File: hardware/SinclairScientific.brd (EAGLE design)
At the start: 47 x 108 mm, 93 parts, among them J1 JSTPH, J3 USB-MICRO, U2 SPX3819-3.3, U3 MCP73831T-2ACI/OT, U4 ATSAMD21G18, U5 W25Q128JVSO, X2 32.768

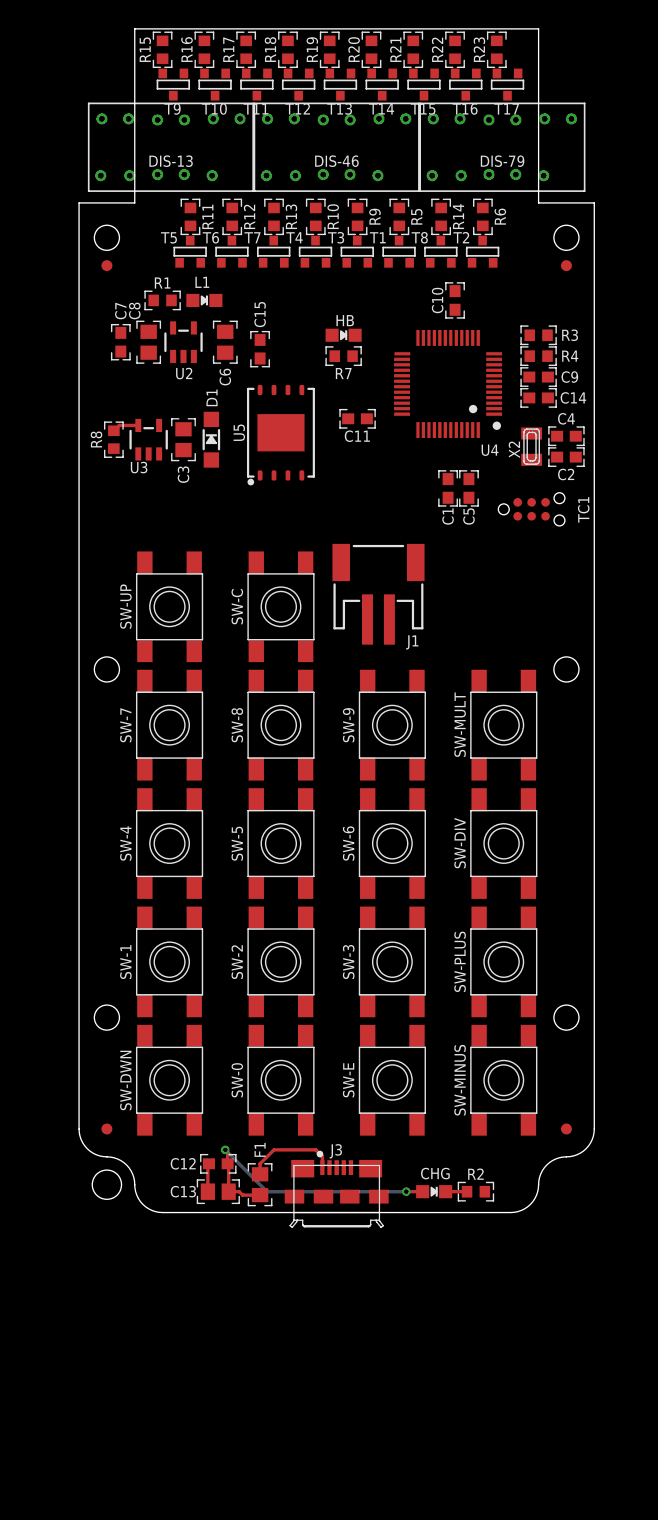
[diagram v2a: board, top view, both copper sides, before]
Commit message: Moved displays to their own sch/brd files, nearly finished routing main board
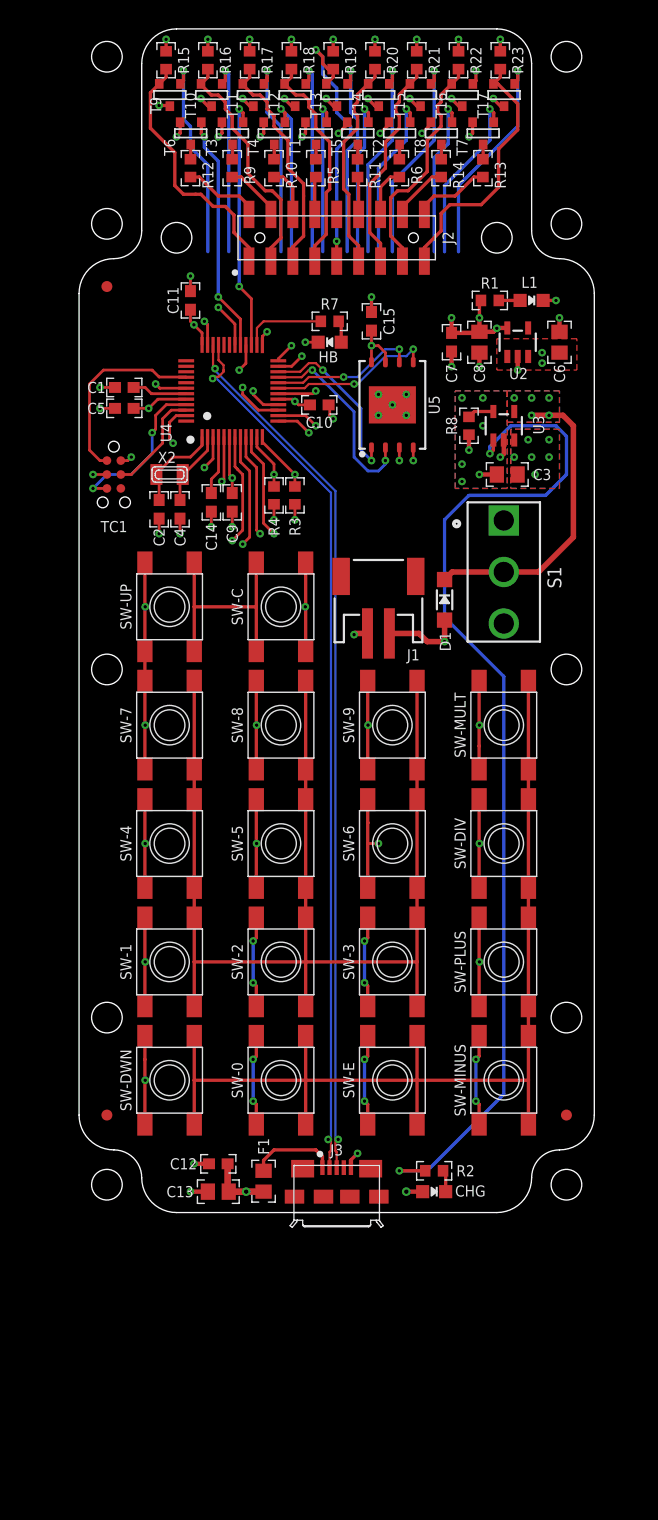
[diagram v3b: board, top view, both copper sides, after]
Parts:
- removed DIS-13, DIS-46, DIS-79: LED_3X7-SEGMENT, SinclairScientific:2352B
- removed U$34: FIDUCIAL"", SinclairScientific:FIDUCIAL_1MM
- added J2: (no value), SinclairScientific:2X09-2MM-SMD
- added S1: SPST_SLIDE, SinclairScientific:SW_1101M2S3CQE2
- added U$14, U$17, U$18, U$19, U$20, U$23, U$24, U$25, U$26, U$27, U$28, U$31: (no value), SinclairScientific:HOLE_3-48
- R2: value 2.2k -> 1k
- R8: value 10K\ -> 3.3k
- moved U$2 42.0 mm to (2.54, 84.5)
- moved TC1 38.2 mm to (3.17, 67.3), turned to 270 degrees
- moved C2 37.5 mm to (7.30, 64.1), turned to 270 degrees
- moved C4 35.9 mm to (9.21, 64.1), turned to 270 degrees
- moved X2 33.1 mm to (8.26, 67.3), turned to 180 degrees
- moved R8 32.4 mm to (35.6, 71.8)
- moved U3 32.4 mm to (38.7, 71.8)
- moved C5 32.3 mm to (4.13, 73.3), turned to 180 degrees
- moved C14 31.3 mm to (12.1, 64.8), turned to 270 degrees
- moved C1 30.9 mm to (4.13, 75.2), turned to 180 degrees
- moved U2 30.5 mm to (40.0, 79.4)
- moved C6 30.5 mm to (43.8, 79.4)
- moved C9 30.2 mm to (14.0, 64.8), turned to 270 degrees
- moved C8 30.2 mm to (36.5, 79.4)
- moved C7 30.2 mm to (34.0, 79.4)
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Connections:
- net D39 renamed D39/!MEM_CS
- net N$5 renamed EXTAL32
- net N$7 renamed XTAL32
- net USB_DM renamed USBD_N
- net USB_DP renamed USBD_P
- removed net LED_A: DIS-13.11, DIS-46.11, DIS-79.11, R5.1
- removed net LED_B: DIS-13.7, DIS-46.7, DIS-79.7, R6.1
- removed net LED_C: DIS-13.4, DIS-46.4, DIS-79.4, R9.1
- removed net LED_CA1: DIS-13.12, R15.1, T9.2
- removed net LED_CA2: DIS-13.9, R16.1, T10.2
- removed net LED_CA3: DIS-13.8, R17.1, T11.2
- removed net LED_CA4: DIS-46.12, R18.1, T12.2
- removed net LED_CA5: DIS-46.9, R19.1, T13.2
- removed net LED_CA6: DIS-46.8, R20.1, T14.2
- removed net LED_CA7: DIS-79.12, R21.1, T15.2
- removed net LED_CA8: DIS-79.9, R22.1, T16.2
- removed net LED_CA9: DIS-79.8, R23.1, T17.2
- removed net LED_D: DIS-13.2, DIS-46.2, DIS-79.2, R10.1
- removed net LED_DP: DIS-13.3, DIS-46.3, DIS-79.3, R14.1
- removed net LED_E: DIS-13.1, DIS-46.1, DIS-79.1, R11.1
- removed net LED_F: DIS-13.10, DIS-46.10, DIS-79.10, R12.1
- removed net LED_G: DIS-13.5, DIS-46.5, DIS-79.5, R13.1
- new net A: J2.8, R5.1
- new net B: J2.14, R6.1
- new net C: J2.4, R9.1
- new net CA1: J2.1, R15.1, T9.2
- new net CA2: J2.3, R16.1, T10.2
- new net CA3: J2.5, R17.1, T11.2
- new net CA4: J2.7, R18.1, T12.2
- new net CA5: J2.9, R19.1, T13.2
- new net CA6: J2.11, R20.1, T14.2
- new net CA7: J2.13, R21.1, T15.2
- new net CA8: J2.15, R22.1, T16.2
- new net CA9: J2.17, R23.1, T17.2
- new net D: J2.6, R10.1
- new net DP: J2.16, R14.1
- new net E: J2.12, R11.1
- new net F: J2.2, R12.1
- new net G: J2.18, R13.1
- new net VBUS_SW: C6.1, S1.1, U2.1, U2.3
- net D0: now also T2.3
- net D1: now also T5.3
- net D8/A6: no longer T2.3
- net D9/A7: no longer T5.3
- net VBUS: now also S1.2; no longer C6.1, U2.1, U2.3
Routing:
- net D8/A6: track 0.00 -> 121.8 mm, vias 0 -> 1
- net D9/A7: track 0.00 -> 114.8 mm, vias 0 -> 1
- net N$3: track 0.00 -> 95.9 mm, vias 0 -> 2
- net VBUS: track 26.5 -> 112.4 mm, vias 2 -> 7
- net USBD_N: track 0.00 -> 81.4 mm, vias 0 -> 2
- net USBD_P: track 0.00 -> 80.4 mm, vias 0 -> 2
- net GND: track 2.58 -> 69.8 mm, vias 0 -> 57
- net D17/A3: track 0.00 -> 46.2 mm, vias 0 -> 4
- net D15/A1: track 0.00 -> 45.8 mm, vias 0 -> 5
- net +3V3: track 0.00 -> 45.5 mm, vias 0 -> 19
- net D16/A2: track 0.00 -> 45.1 mm, vias 0 -> 5
- net D7: track 0.00 -> 39.1 mm, vias 0 -> 5
- net D12: track 0.00 -> 38.9 mm, vias 0 -> 5
- net D4: track 0.00 -> 38.6 mm, vias 0 -> 4
- net D3: track 0.00 -> 37.8 mm, vias 0 -> 4
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- added copper zone on layer 15, net +3V3
- added copper zone on layer 1, net GND
- added copper zone on layer 16, net GND
- added copper zone on layer 2, net GND
- added copper zone on layer 1, net VBAT
- added copper zone on layer 16, net VBAT
- added copper zone on layer 1, net VBUS
- added copper zone on layer 16, net VBUS
- added copper zone on layer 1, net VBUS_SW
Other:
- outline, holes or cut-outs redrawn

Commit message: Finished routing
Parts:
- removed U$17, U$18, U$19, U$20, U$28, U$31: (no value), SinclairScientific:HOLE_3-48
- moved C11 5.43 mm to (5.08, 81.3), turned to 180 degrees
- moved R3 0.64 mm to (19.7, 64.8)
- moved R4 0.64 mm to (17.8, 64.8)
- moved U$14 0.63 mm to (8.89, 89.5)
- moved U$23 0.63 mm to (38.1, 89.5)
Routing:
- net D12: track 38.9 -> 184.4 mm, vias 5 -> 8
- net D11: track 19.0 -> 133.6 mm, vias 5 -> 10
- net D3: track 37.8 -> 145.9 mm, vias 4 -> 9
- net D16/A2: track 45.1 -> 151.5 mm, vias 5 -> 7
- net D15/A1: track 45.8 -> 145.4 mm, vias 5 -> 7
- net D7: track 39.1 -> 136.9 mm, vias 5 -> 6
- net D2: track 37.3 -> 117.3 mm
- net D4: track 38.6 -> 118.1 mm, vias 4 -> 5
- net D17/A3: track 46.2 -> 110.7 mm, vias 4 -> 5
- net D8/A6: track 121.8 -> 167.0 mm, vias 1 -> 2
- net D18/A4: track 24.6 -> 63.9 mm, vias 2 -> 3
- net D14/A0: track 19.2 -> 50.7 mm, vias 2 -> 3
- net D19/A5: track 18.6 -> 48.2 mm, vias 2 -> 4
- net D9/A7: track 114.8 -> 137.6 mm, vias 1 -> 2
- net D0: track 18.4 -> 37.5 mm, vias 2 -> 3
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
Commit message: Added some silkscreen labels and logo
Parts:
- added U$17: (no value), SinclairScientific:LOGO_PLH_2700
- added U$18: SILK_QC, SinclairScientific:SILK_QC
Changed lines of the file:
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@@
 <layer number="25" name="tNames" color="7" fill="1" visible="yes" active="yes"/>
 <layer number="26" name="bNames" color="7" fill="1" visible="yes" active="yes"/>
-<layer number="27" name="tValues" color="7" fill="1" visible="no" active="yes"/>
+<layer number="27" name="tValues" color="7" fill="1" visible="yes" active="yes"/>
 <layer number="28" name="bValues" color="7" fill="1" visible="no" active="yes"/>
 <layer number="29" name="tStop" color="7" fill="3" visible="no" active="yes"/>
@@
 <layer number="112" name="tSilk" color="7" fill="1" visible="no" active="yes"/>
 <layer number="113" name="ReferenceLS" color="7" fill="1" visible="no" active="no"/>
+<layer number="114" name="Badge_Outline" color="7" fill="1" visible="no" active="yes"/>
+<layer number="115" name="ReferenceISLANDS" color="7" fill="1" visible="no" active="yes"/>
 <layer number="116" name="Patch_BOT" color="9" fill="4" visible="no" active="yes"/>
 <layer number="118" name="Rect_Pads" color="7" fill="1" visible="no" active="no"/>
@@
 </plain>
 <attributes>
-<attribute name="REV" value="C"/>
 </attributes>
 <variantdefs>
@@
 <attribute name="NAME" x="36.5125" y="76.5175" size="1.016" layer="25" font="vector" ratio="20" rot="R270" align="center"/>
 <attribute name="PN-DK" value="" x="36.5125" y="79.375" size="1.778" layer="27" rot="R270" display="off"/>
-<attribute name="REV" value="A" x="36.5125" y="79.375" size="1.778" layer="27" rot="R270" display="off"/>
 <attribute name="VALUE" x="36.5125" y="79.375" size="1.016" layer="27" font="vector" ratio="20" rot="R270" align="center"/>
 </element>
@@
 <attribute name="VALUE" x="44.10476875" y="53.01066875" size="1.27156875" layer="27" rot="R90"/>
 </element>
+<element name="U$18" library="SinclairScientific" package="SILK_QC" value="SILK_QC" x="23.495" y="94.615" rot="MR0">
+<attribute name="MPN" value="DNP" x="23.495" y="94.615" size="1.778" layer="28" rot="MR0" display="off"/>
+<attribute name="PRODUCT" value="SinclairScientific" x="23.495" y="99.695" size="2.032" layer="22" font="vector" ratio="15" rot="MR0" align="center"/>
+<attribute name="REV" value="1B" x="20.955" y="95.885" size="2.032" layer="22" font="vector" ratio="15" rot="MR0" align="center-left"/>
+</element>
+<element name="U$17" library="SinclairScientific" package="LOGO_PLH_2700" value="" x="23.1775" y="42.545" rot="MR270"/>
 </elements>
 <signals>

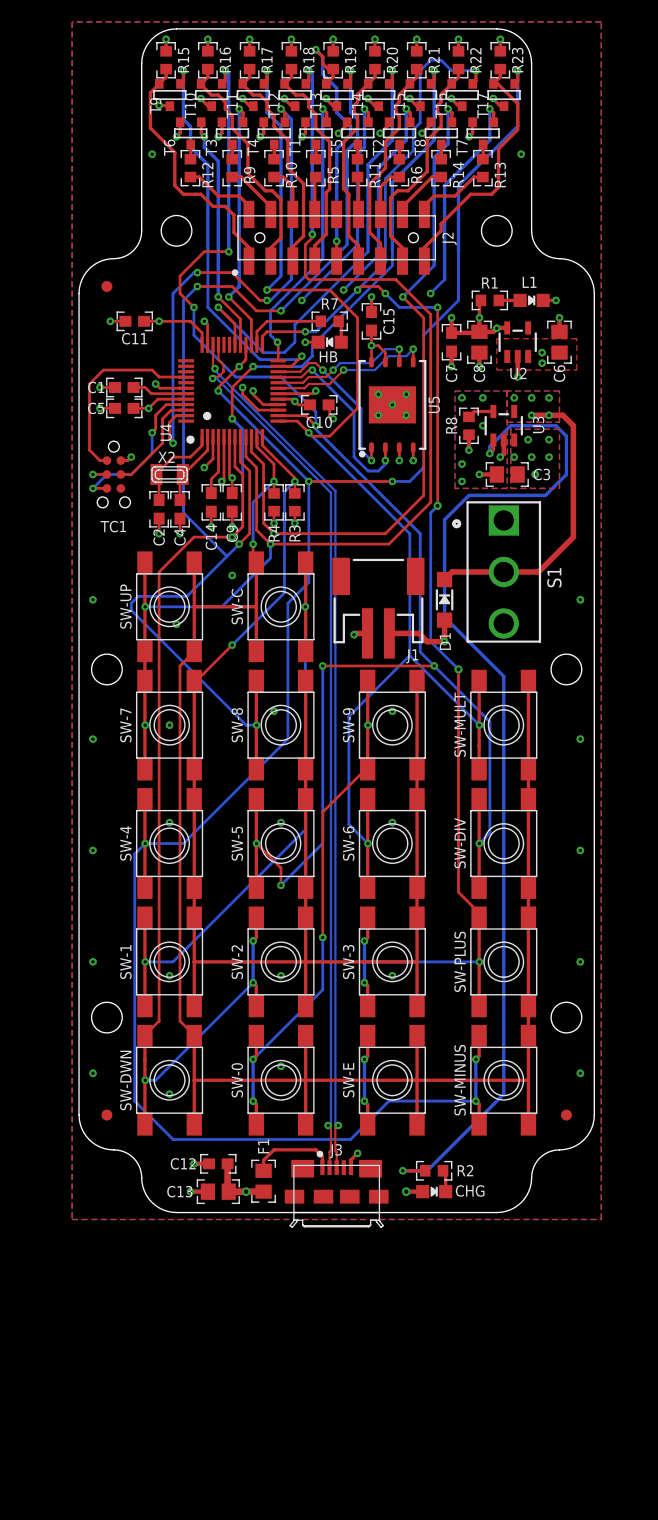
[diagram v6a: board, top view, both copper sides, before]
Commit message: Converted local library to managed library. Fixed more hardware issues found from testing v1B prototype.
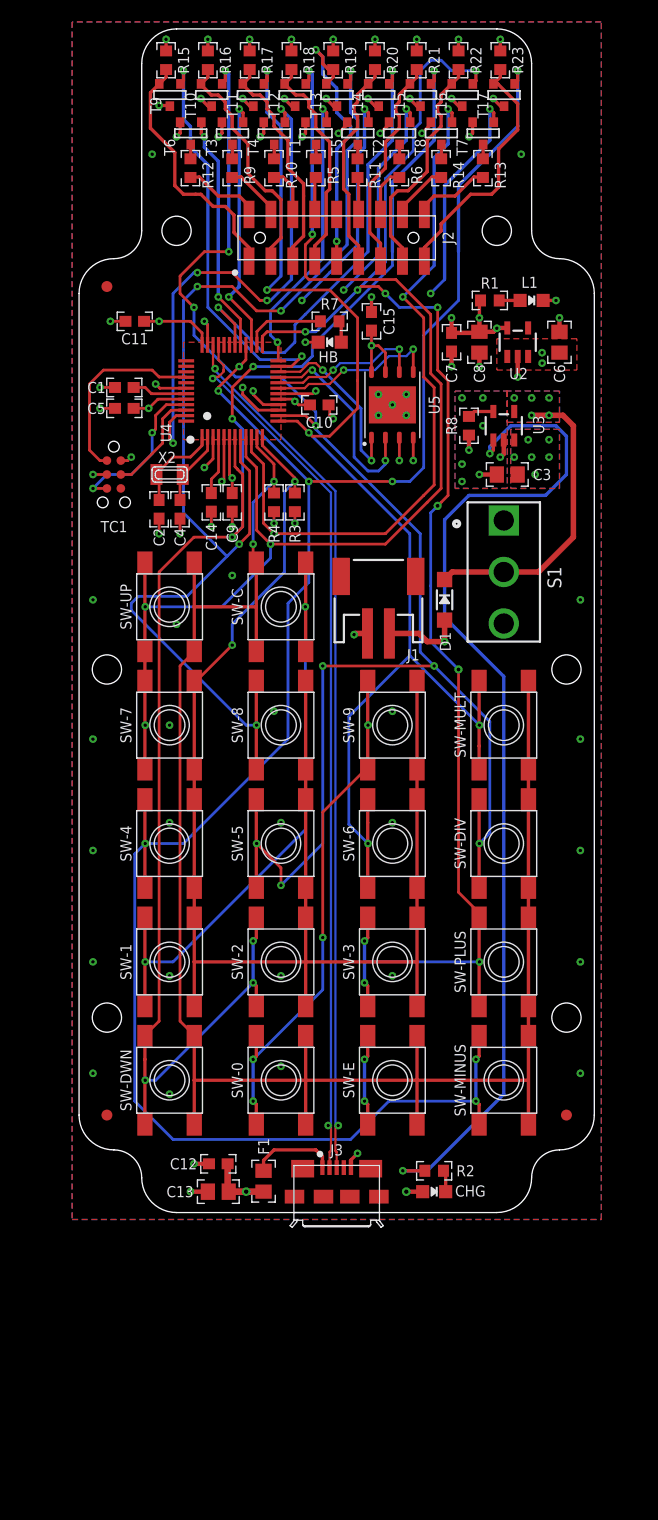
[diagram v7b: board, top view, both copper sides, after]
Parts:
- added U$19, U$20, U$28, U$31, U$32, U$33, U$34, U$37, U$40, U$41, U$42, U$43, U$44, U$45, U$46, U$47, U$48, U$49: SW-CAP_1SWXXX, SinclairScientific:SW-CAP_1SWXXX
- U5: value W25Q128JVSO -> W25Q128JVWSON_6X5; device SinclairScientific:SON127P800X600X80-9N -> SinclairScientific:SON127P600X500X80-9N
- renumbered U$14 to U$55, U$23 to U$54, U$24 to U$50, U$25 to U$53, U$26 to U$52, U$27 to U$51
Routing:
- net +3V3: track 48.7 -> 51.4 mm
- net D24/SCK: track 13.5 -> 14.4 mm
- net D23/MOSI: track 15.0 -> 15.9 mm
- net D39/!MEM_CS: track 15.9 -> 16.8 mm
- net D22/MISO: track 18.0 -> 18.9 mm
- net D11: track 133.6 -> 134.4 mm
- net D18/A4: track 63.9 -> 64.7 mm
- net D17/A3: track 110.7 -> 111.3 mm

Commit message: Changed on/off switch to SMD type, fixed some DFM issues
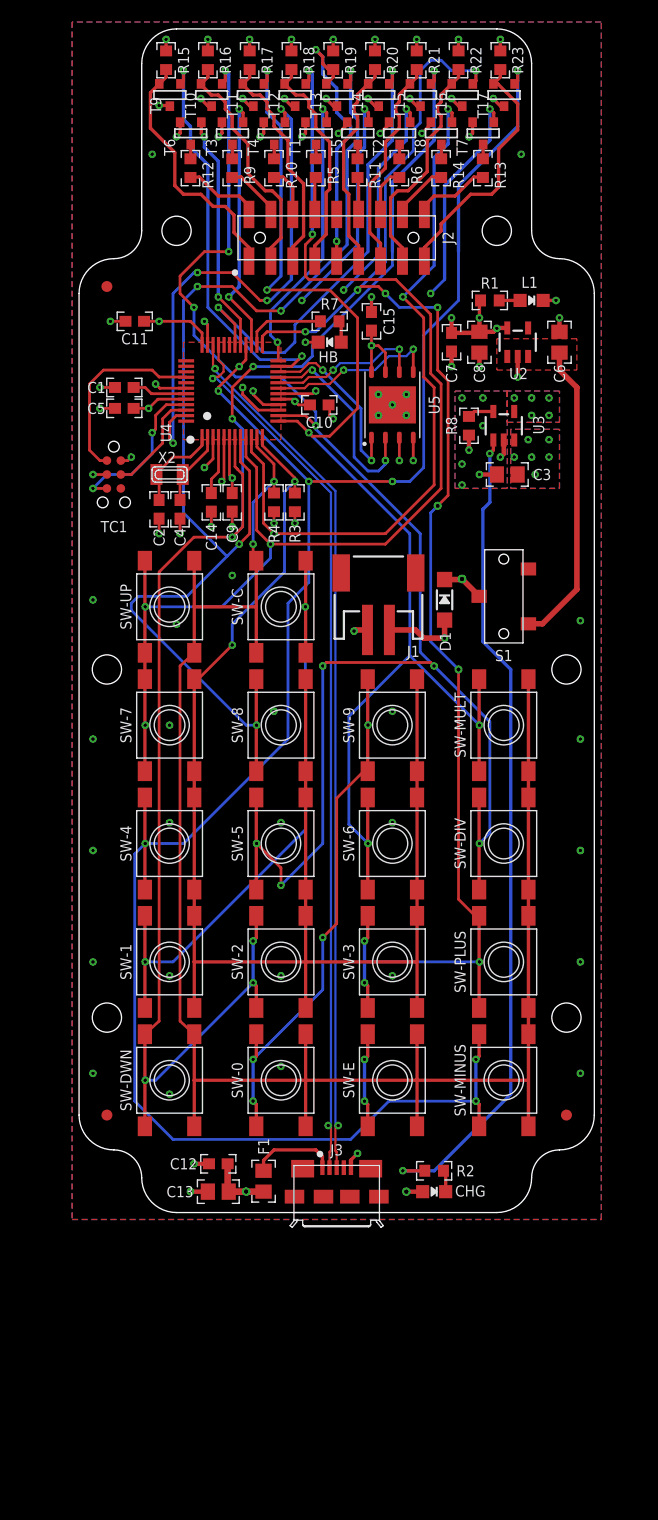
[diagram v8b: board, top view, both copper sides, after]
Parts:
- S1: value SPST_SLIDE -> SPDT_SLIDE-CB-SB-12B; device SinclairScientific:SW_1101M2S3CQE2 -> SinclairScientific:CL-SB-12B
- moved S1 2.22 mm to (38.7, 56.2), turned to 90 degrees
- moved J1 0.32 mm to (27.3, 56.8)
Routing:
- net N$3: track 95.2 -> 75.9 mm
- net VBUS_SW: track 19.5 -> 28.0 mm, vias 2 -> 0
- net VBUS: track 112.4 -> 115.2 mm, vias 7 -> 8
- net D8/A6: track 167.0 -> 169.2 mm
- net VBAT: track 28.4 -> 26.3 mm
- net D9/A7: track 137.6 -> 138.8 mm
- net D3: track 145.9 -> 147.0 mm
- net D7: track 136.9 -> 137.8 mm
- net D4: track 118.1 -> 118.9 mm
- net D12: track 184.4 -> 185.2 mm
- net D2: track 117.3 -> 118.1 mm
- net D16/A2: track 151.5 -> 152.3 mm
- net D11: track 134.4 -> 135.2 mm
- net D15/A1: track 145.4 -> 146.0 mm
- added copper zone on layer 15, net VBAT
- added copper zone on layer 15, net VBUS
